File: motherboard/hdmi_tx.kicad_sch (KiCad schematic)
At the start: 49 parts, among them J8 HDMI_A, Q1 2SK3018W, Q2 2SK3018W, Q3 L2N7002WT1G, Q4 2SK3018W, Q5 2SK3018W, Q6 WNM6002-3/TR, Q7 WNM6002-3/TR, Q8 WNM6002-3/TR, Q9 WNM6002-3/TR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

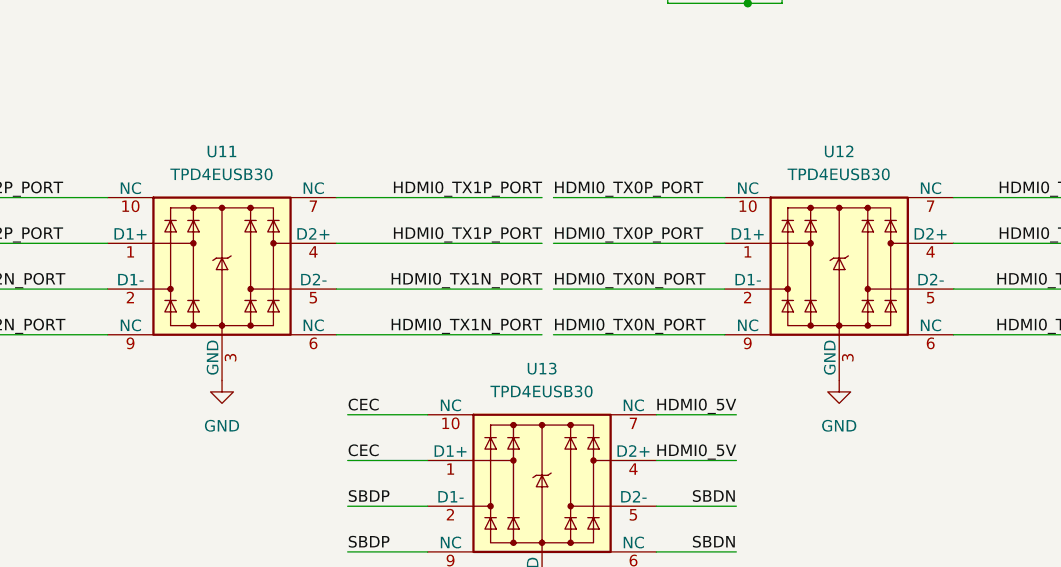
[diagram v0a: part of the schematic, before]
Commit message: placement roughly halfway done
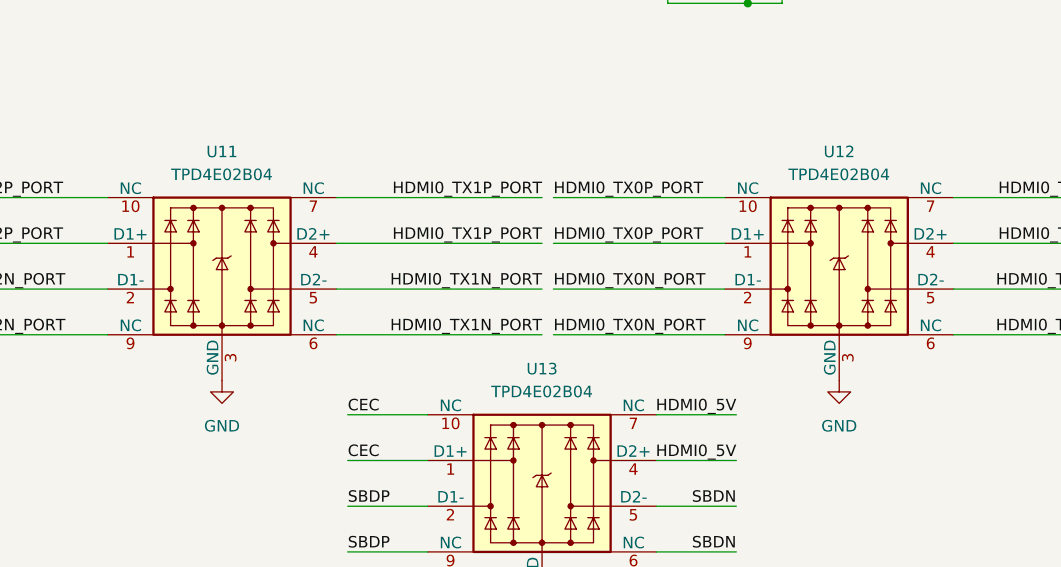
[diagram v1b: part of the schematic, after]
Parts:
- U11, U12, U13: value TPD4EUSB30 -> TPD4E02B04
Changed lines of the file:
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@@
 			)
 		)
-		(property "Value" "TPD4EUSB30"
+		(property "Value" "TPD4E02B04"
 			(at 121.92 137.16 0)
 			(effects
@@
 			)
 		)
-		(property "Value" "TPD4EUSB30"
+		(property "Value" "TPD4E02B04"
 			(at 88.9 161.29 0)
 			(effects
@@
 			)
 		)
-		(property "Value" "TPD4EUSB30"
+		(property "Value" "TPD4E02B04"
 			(at 53.34 137.16 0)
 			(effects

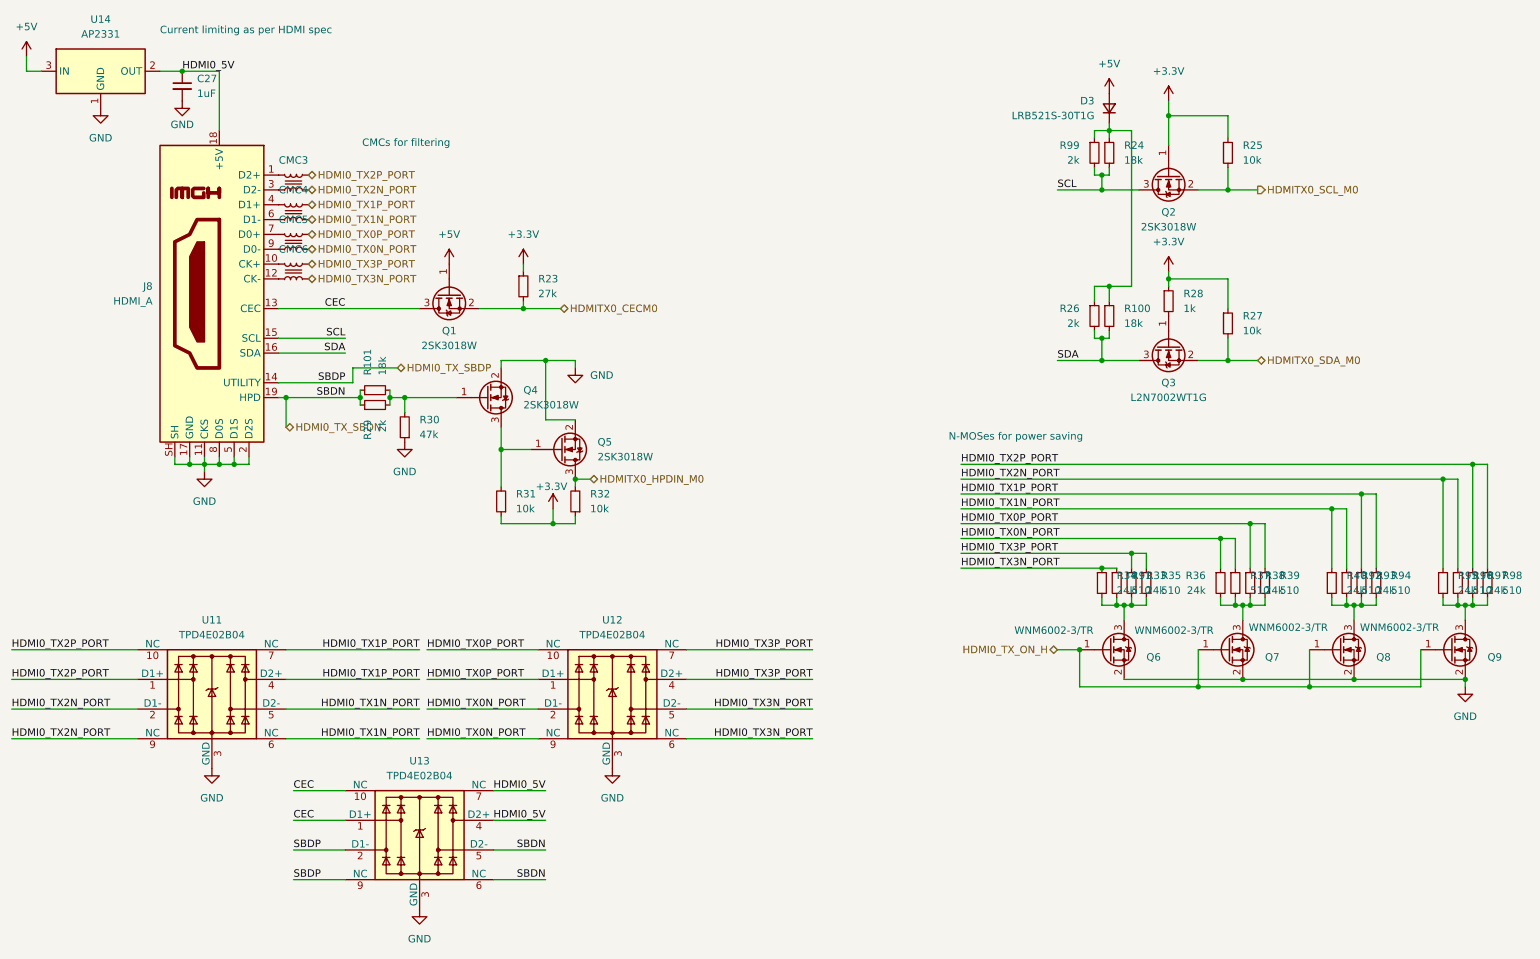
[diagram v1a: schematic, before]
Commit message: motherboard net labeling and impedance matching
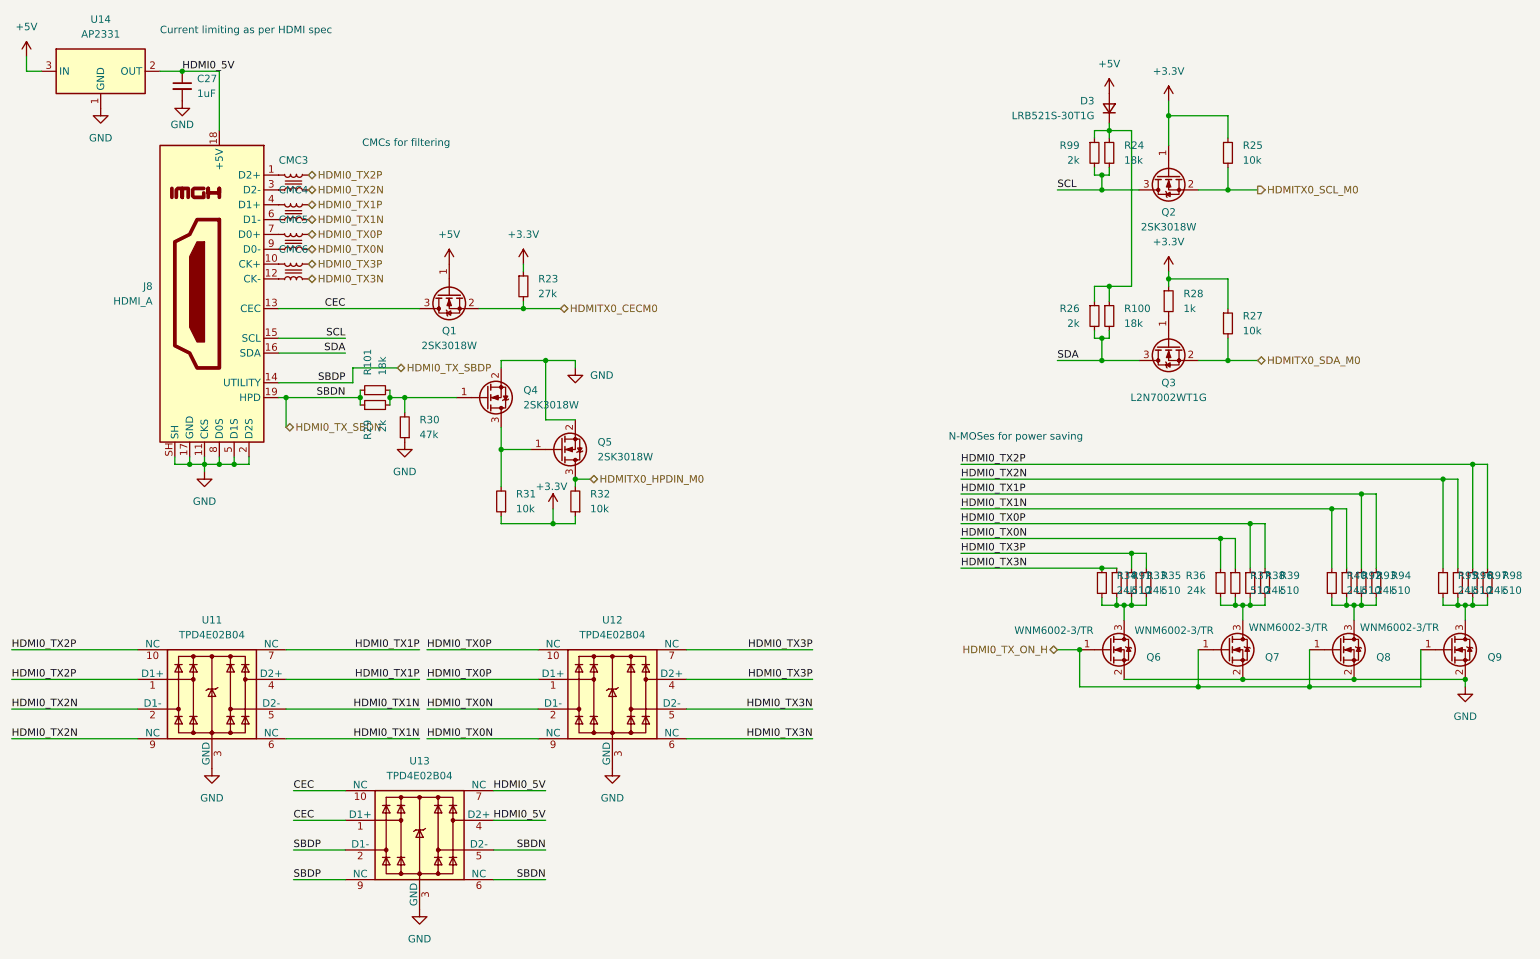
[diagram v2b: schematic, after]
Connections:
- net HDMI0_TX0N_PORT renamed HDMI0_TX0N
- net HDMI0_TX0P_PORT renamed HDMI0_TX0P
- net HDMI0_TX1N_PORT renamed HDMI0_TX1N
- net HDMI0_TX1P_PORT renamed HDMI0_TX1P
- net HDMI0_TX2N_PORT renamed HDMI0_TX2N
- net HDMI0_TX2P_PORT renamed HDMI0_TX2P
- net HDMI0_TX3N_PORT renamed HDMI0_TX3N
- net HDMI0_TX3P_PORT renamed HDMI0_TX3P
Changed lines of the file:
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@@
 		)
 	)
-	(label "HDMI0_TX1P_PORT"
+	(label "HDMI0_TX1P"
 		(at 88.9 139.7 180)
 		(fields_autoplaced yes)
@@
 		)
 	)
-	(label "HDMI0_TX3P_PORT"
+	(label "HDMI0_TX3P"
 		(at 156.21 139.7 180)
 		(fields_autoplaced yes)
@@
 		)
 	)
-	(label "HDMI0_TX3N_PORT"
+	(label "HDMI0_TX3N"
 		(at 156.21 149.86 180)
 		(fields_autoplaced yes)
@@
 		)
 	)
-	(label "HDMI0_TX2N_PORT"
+	(label "HDMI0_TX2N"
 		(at 19.05 149.86 0)
 		(fields_autoplaced yes)
@@
 		)
 	)
-	(label "HDMI0_TX0P_PORT"
+	(label "HDMI0_TX0P"
 		(at 90.17 139.7 0)
 		(fields_autoplaced yes)
@@
 		)
 	)
-	(label "HDMI0_TX2P_PORT"
+	(label "HDMI0_TX2P"
 		(at 19.05 144.78 0)
 		(fields_autoplaced yes)
@@
 		)
 	)
-	(label "HDMI0_TX2P_PORT"
+	(label "HDMI0_TX2P"
 		(at 181.61 107.95 0)
 		(fields_autoplaced yes)
@@
 		)
 	)
-	(label "HDMI0_TX3P_PORT"
+	(label "HDMI0_TX3P"
 		(at 181.61 123.19 0)
 		(fields_autoplaced yes)
@@
 		)
 	)
-	(label "HDMI0_TX1N_PORT"
+	(label "HDMI0_TX1N"
 		(at 181.61 115.57 0)
 		(fields_autoplaced yes)
@@
 		)
 	)
-	(label "HDMI0_TX1N_PORT"
+	(label "HDMI0_TX1N"
 		(at 88.9 149.86 180)
 		(fields_autoplaced yes)
@@
 		)
 	)
-	(label "HDMI0_TX0N_PORT"
+	(label "HDMI0_TX0N"
 		(at 181.61 120.65 0)
 		(fields_autoplaced yes)
@@
 		)
 	)
-	(label "HDMI0_TX1P_PORT"
+	(label "HDMI0_TX1P"
 		(at 181.61 113.03 0)
 		(fields_autoplaced yes)
@@
 		)
 	)
-	(label "HDMI0_TX2N_PORT"
+	(label "HDMI0_TX2N"
 		(at 181.61 110.49 0)
 		(fields_autoplaced yes)
@@
 		)
 	)
-	(label "HDMI0_TX0N_PORT"
+	(label "HDMI0_TX0N"
 		(at 90.17 149.86 0)
 		(fields_autoplaced yes)
@@
 		)
 	)
-	(label "HDMI0_TX0P_PORT"
+	(label "HDMI0_TX0P"
 		(at 181.61 118.11 0)
 		(fields_autoplaced yes)
@@
 		)
 	)
-	(label "HDMI0_TX3N_PORT"
+	(label "HDMI0_TX3N"
 		(at 156.21 154.94 180)
 		(fields_autoplaced yes)
@@
 		)
 	)
-	(label "HDMI0_TX3N_PORT"
+	(label "HDMI0_TX3N"
 		(at 181.61 125.73 0)
 		(fields_autoplaced yes)
@@
 		)
 	)
-	(label "HDMI0_TX2N_PORT"
+	(label "HDMI0_TX2N"
 		(at 19.05 154.94 0)
 		(fields_autoplaced yes)
@@
 		)
 	)
-	(label "HDMI0_TX1P_PORT"
+	(label "HDMI0_TX1P"
 		(at 88.9 144.78 180)
 		(fields_autoplaced yes)
@@
 		)
 	)
-	(label "HDMI0_TX0N_PORT"
+	(label "HDMI0_TX0N"
 		(at 90.17 154.94 0)
 		(fields_autoplaced yes)
@@
 		)
 	)
-	(label "HDMI0_TX3P_PORT"
+	(label "HDMI0_TX3P"
 		(at 156.21 144.78 180)
 		(fields_autoplaced yes)
@@
 		)
 	)
-	(label "HDMI0_TX2P_PORT"
+	(label "HDMI0_TX2P"
 		(at 19.05 139.7 0)
 		(fields_autoplaced yes)
@@
 		)
 	)
-	(label "HDMI0_TX0P_PORT"
+	(label "HDMI0_TX0P"
 		(at 90.17 144.78 0)
 		(fields_autoplaced yes)
@@
 		)
 	)
-	(label "HDMI0_TX1N_PORT"
+	(label "HDMI0_TX1N"
 		(at 88.9 154.94 180)
 		(fields_autoplaced yes)
@@
 		)
 	)
-	(hierarchical_label "HDMI0_TX1P_PORT"
+	(hierarchical_label "HDMI0_TX1P"
 		(shape bidirectional)
 		(at 69.85 63.5 0)
@@
 		)
 	)
-	(hierarchical_label "HDMI0_TX0N_PORT"
+	(hierarchical_label "HDMI0_TX0N"
 		(shape bidirectional)
 		(at 69.85 71.12 0)
@@
 		)
 	)
-	(hierarchical_label "HDMI0_TX0P_PORT"
+	(hierarchical_label "HDMI0_TX0P"
 		(shape bidirectional)
 		(at 69.85 68.58 0)
@@
 		)
 	)
-	(hierarchical_label "HDMI0_TX2N_PORT"
+	(hierarchical_label "HDMI0_TX2N"
 		(shape bidirectional)
 		(at 69.85 60.96 0)
@@
 		)
 	)
-	(hierarchical_label "HDMI0_TX3P_PORT"
+	(hierarchical_label "HDMI0_TX3P"
 		(shape bidirectional)
 		(at 69.85 73.66 0)
@@
 		)
 	)
-	(hierarchical_label "HDMI0_TX2P_PORT"
+	(hierarchical_label "HDMI0_TX2P"
 		(shape bidirectional)
 		(at 69.85 58.42 0)
@@
 		)
 	)
-	(hierarchical_label "HDMI0_TX3N_PORT"
+	(hierarchical_label "HDMI0_TX3N"
 		(shape bidirectional)
 		(at 69.85 76.2 0)
@@
 		)
 	)
-	(hierarchical_label "HDMI0_TX1N_PORT"
+	(hierarchical_label "HDMI0_TX1N"
 		(shape bidirectional)
 		(at 69.85 66.04 0)
